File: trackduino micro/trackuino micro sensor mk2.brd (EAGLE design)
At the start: 43.3 x 19 mm, 44 parts, among them IC2 74AHC1G125DBV, SW1 SPST_TACT-KMR2, U1 ATMEGA168MLF, Y1 16MHZ

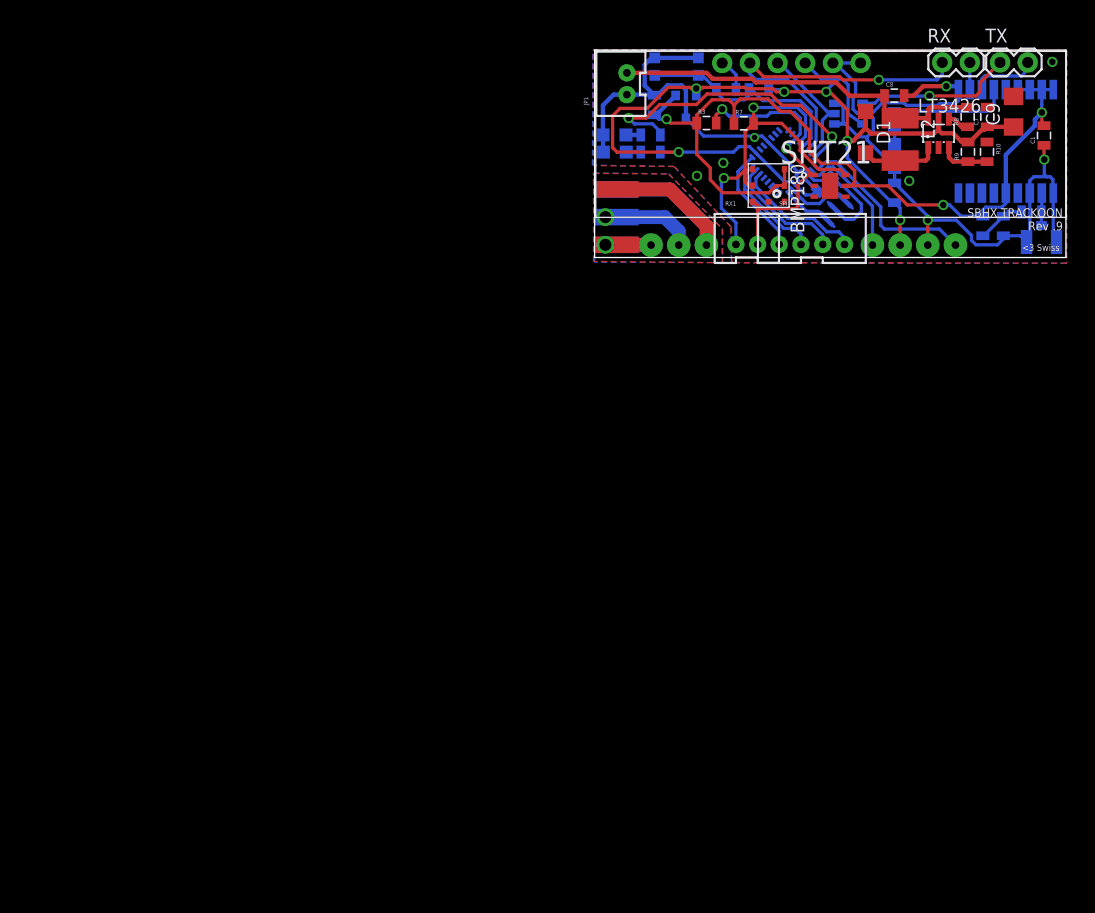
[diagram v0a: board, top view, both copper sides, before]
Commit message: Moved all boards to origin
Moved all the boards such that the lower left most corner is at the
origin.
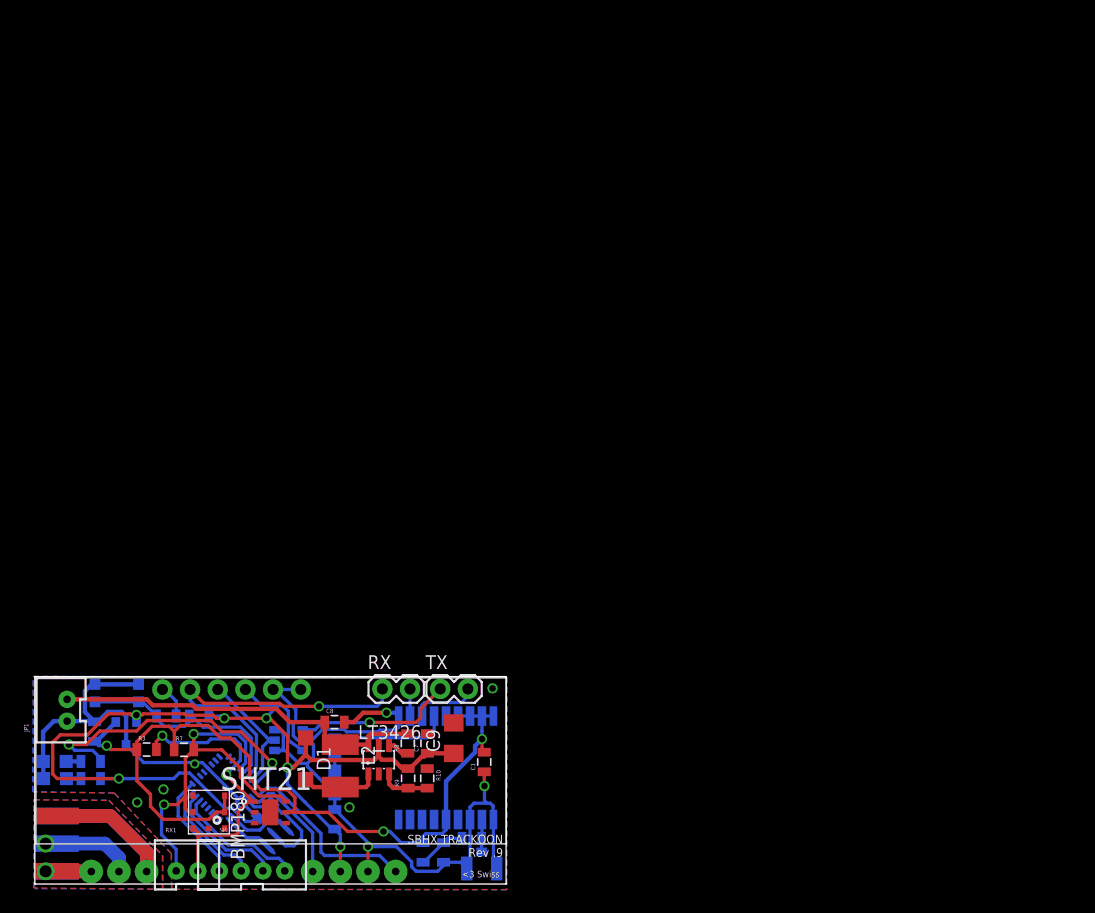
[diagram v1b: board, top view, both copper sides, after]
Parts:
- moved C5 77.1 mm to (12.1, 15.4)
- moved R4 77.1 mm to (5.13, 9.68)
- moved R5 77.1 mm to (15.1, 15.4)
- moved VCC 77.1 mm to (1.85, 9.68)
- moved BMP180 77.1 mm to (16.0, 6.60)
- moved C1 77.1 mm to (41.2, 11.2)
- moved C2 77.1 mm to (5.49, 14.0)
- moved C3 77.1 mm to (21.2, 6.76)
- moved C4 77.1 mm to (27.5, 5.94)
- moved C6 77.1 mm to (37.5, 2.90)
- moved C7 77.1 mm to (36.0, 12.9)
- moved C8 77.1 mm to (27.5, 14.9)
- moved C9 77.1 mm to (38.5, 13.4)
- moved D1 77.1 mm to (24.9, 11.5)
- moved FRAME1 77.1 mm to (14.4, -8.15)
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
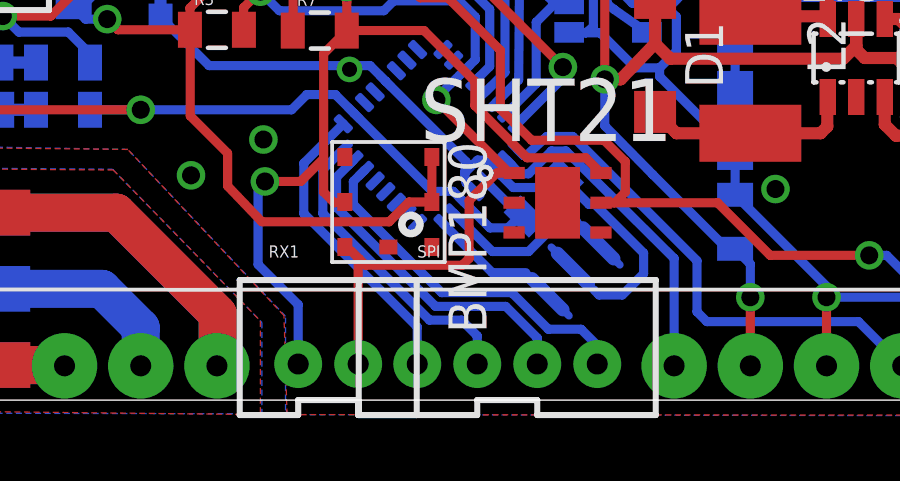
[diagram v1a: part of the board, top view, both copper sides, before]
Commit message: lined up 12c / spi headers
lined up api and i2c headers between the chip, u.fl, and solar versions
of the board.
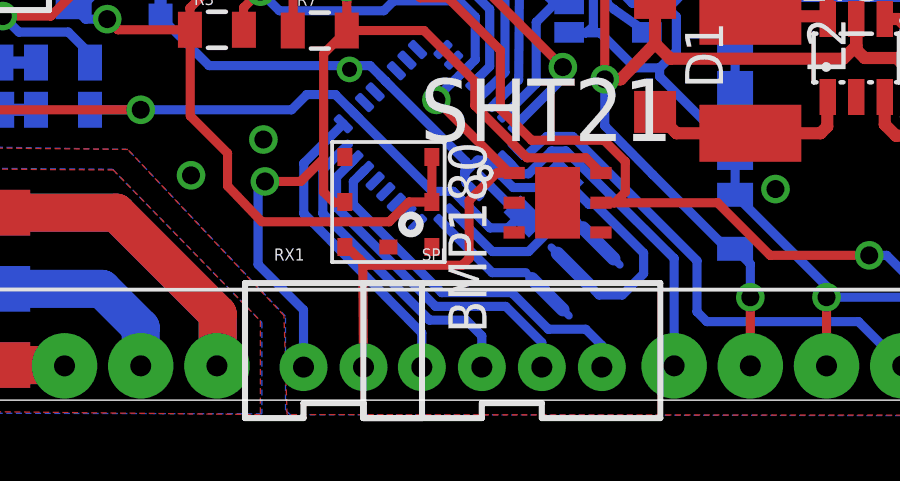
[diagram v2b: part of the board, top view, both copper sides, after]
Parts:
- moved RX1 0.20 mm to (14.1, 1.65)
- moved SPI 0.18 mm to (20.1, 1.65)
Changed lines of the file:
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@@
 <element name="C5" library="SparkFun-Capacitors" package="0805" value=".1uf" x="12.071159375" y="15.427575" rot="MR0"/>
 <element name="TX" library="SparkFun-Connectors" package="1X02" value="TX" x="37.211" y="17.907"/>
-<element name="SPI" library="SparkFun-Connectors" package="JST-4-PTH-VERT" value="" x="19.939" y="1.7526"/>
+<element name="SPI" library="SparkFun-Connectors" package="JST-4-PTH-VERT" value="" x="20.0914" y="1.651"/>
 <element name="FRAME1" library="SparkFun-Aesthetics" package="CREATIVE_COMMONS" value="FRAME-LETTER" x="14.3764" y="-8.1534"/>
 <element name="PTT" library="adafruit" package="CHIP-LED0805" value="" x="1.8288" y="11.2522" rot="MR270"/>
@@
 <attribute name="OC_FARNELL" value="1855468" x="21.6154" y="6.5786" size="1.778" layer="27" display="off"/>
 </element>
-<element name="RX1" library="SparkFun-Connectors" package="JST-2-PTH-VERT" value="RX" x="13.97" y="1.7526"/>
+<element name="RX1" library="SparkFun-Connectors" package="JST-2-PTH-VERT" value="RX" x="14.1478" y="1.651"/>
 </elements>
 <signals>
@@
 <contactref element="U1" pad="16"/>
 <contactref element="SPI" pad="2"/>
-<wire x1="18.939" y1="1.2026" x2="18.939" y2="2.143" width="0.3048" layer="16"/>
-<wire x1="18.939" y1="2.143" x2="18.415" y2="2.667" width="0.3048" layer="16"/>
-<wire x1="18.415" y1="2.667" x2="17.3482" y2="2.667" width="0.3048" layer="16"/>
+<wire x1="19.0914" y1="1.101" x2="19.0914" y2="2.143" width="0.3048" layer="16"/>
+<wire x1="19.0914" y1="2.143" x2="18.5674" y2="2.667" width="0.3048" layer="16"/>
+<wire x1="18.5674" y1="2.667" x2="17.3482" y2="2.667" width="0.3048" layer="16"/>
 <wire x1="17.3482" y1="2.667" x2="13.7922" y2="6.223" width="0.3048" layer="16"/>
 <wire x1="13.7922" y1="6.223" x2="13.7922" y2="7.681871875" width="0.3048" layer="16"/>
@@
 <contactref element="U1" pad="15"/>
 <contactref element="SPI" pad="3"/>
-<wire x1="20.939" y1="1.2026" x2="20.939" y2="2.0734" width="0.3048" layer="16"/>
-<wire x1="20.939" y1="2.0734" x2="19.8882" y2="3.1242" width="0.3048" layer="16"/>
+<wire x1="21.0914" y1="1.101" x2="21.0914" y2="1.921" width="0.3048" layer="16"/>
+<wire x1="21.0914" y1="1.921" x2="19.8882" y2="3.1242" width="0.3048" layer="16"/>
 <wire x1="19.8882" y1="3.1242" x2="17.5514" y2="3.1242" width="0.3048" layer="16"/>
 <wire x1="17.5514" y1="3.1242" x2="14.2494" y2="6.4262" width="0.3048" layer="16"/>
@@
 <contactref element="U1" pad="17"/>
 <contactref element="SPI" pad="1"/>
-<wire x1="16.939" y1="1.2026" x2="16.939" y2="2.4412" width="0.3048" layer="16"/>
-<wire x1="16.939" y1="2.4412" x2="13.1572" y2="6.223" width="0.3048" layer="16"/>
+<wire x1="17.0914" y1="1.101" x2="17.0914" y2="2.238" width="0.3048" layer="16"/>
+<wire x1="17.0914" y1="2.238" x2="13.1572" y2="6.223" width="0.3048" layer="16"/>
 <wire x1="13.1572" y1="6.223" x2="13.1572" y2="7.8954" width="0.3048" layer="16"/>
 <wire x1="13.1572" y1="7.8954" x2="14.4744625" y2="9.2126625" width="0.3048" layer="16"/>
@@
 <contactref element="U1" pad="14"/>
 <contactref element="SPI" pad="4"/>
-<wire x1="22.939" y1="1.2026" x2="22.939" y2="1.826" width="0.3048" layer="16"/>
-<wire x1="22.939" y1="1.826" x2="22.4028" y2="2.3622" width="0.3048" layer="16"/>
-<wire x1="22.4028" y1="2.3622" x2="21.3106" y2="2.3622" width="0.3048" layer="16"/>
+<wire x1="23.0914" y1="1.101" x2="23.0914" y2="1.826" width="0.3048" layer="16"/>
+<wire x1="23.0914" y1="1.826" x2="22.5552" y2="2.3622" width="0.3048" layer="16"/>
+<wire x1="22.5552" y1="2.3622" x2="21.3106" y2="2.3622" width="0.3048" layer="16"/>
 <wire x1="21.3106" y1="2.3622" x2="20.0914" y2="3.5814" width="0.3048" layer="16"/>
 <wire x1="20.0914" y1="3.5814" x2="17.7546" y2="3.5814" width="0.3048" layer="16"/>
@@
 <wire x1="17.5768" y1="10.07765625" x2="18.504971875" y2="10.980428125" width="0.3048" layer="16"/>
 <contactref element="RX1" pad="2"/>
-<wire x1="14.97" y1="1.2026" x2="14.97" y2="4.683" width="0.3048" layer="1"/>
-<wire x1="14.97" y1="4.683" x2="14.9987" y2="4.7117" width="0.3048" layer="1"/>
+<wire x1="15.1478" y1="1.101" x2="15.1224" y2="4.5814" width="0.3048" layer="1"/>
+<wire x1="15.1224" y1="4.5814" x2="14.9987" y2="4.7117" width="0.3048" layer="1"/>
 </signal>
 <signal name="SCL">
@@
 <wire x1="17.1664" y1="12.319" x2="14.5906" y2="12.319" width="0.3048" layer="1"/>
 <contactref element="RX1" pad="1"/>
-<wire x1="12.97" y1="1.2026" x2="12.97" y2="3.1844" width="0.3048" layer="16"/>
-<wire x1="12.97" y1="3.1844" x2="11.6332" y2="4.5212" width="0.3048" layer="16"/>
+<wire x1="13.1478" y1="1.101" x2="13.1478" y2="3.0066" width="0.3048" layer="16"/>
+<wire x1="13.1478" y1="3.0066" x2="11.6332" y2="4.5212" width="0.3048" layer="16"/>
 <wire x1="11.6332" y1="4.5212" x2="11.6332" y2="7.0612" width="0.3048" layer="16"/>
 <wire x1="11.6332" y1="7.0612" x2="11.8618" y2="7.2898" width="0.3048" layer="16"/>

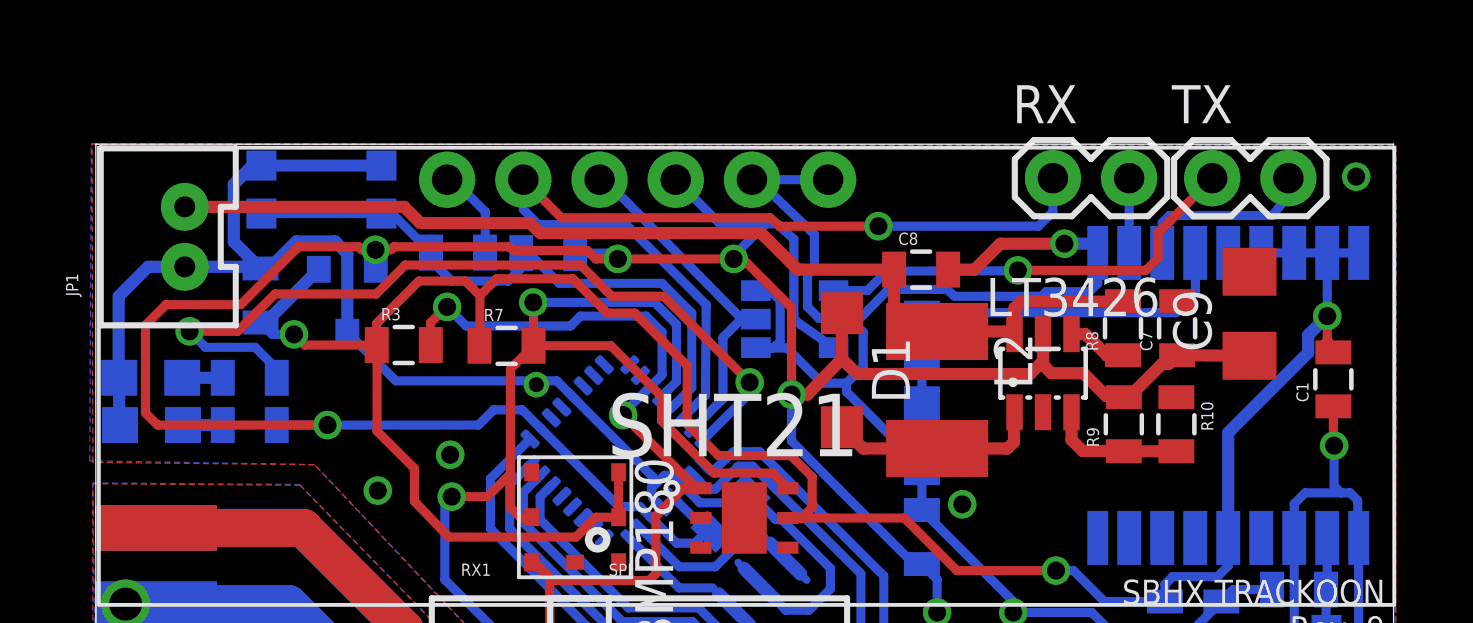
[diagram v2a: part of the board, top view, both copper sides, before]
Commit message: tx rx 2mm headers
replaced .1” serial headers on chip and non chip version with 2mm
headers
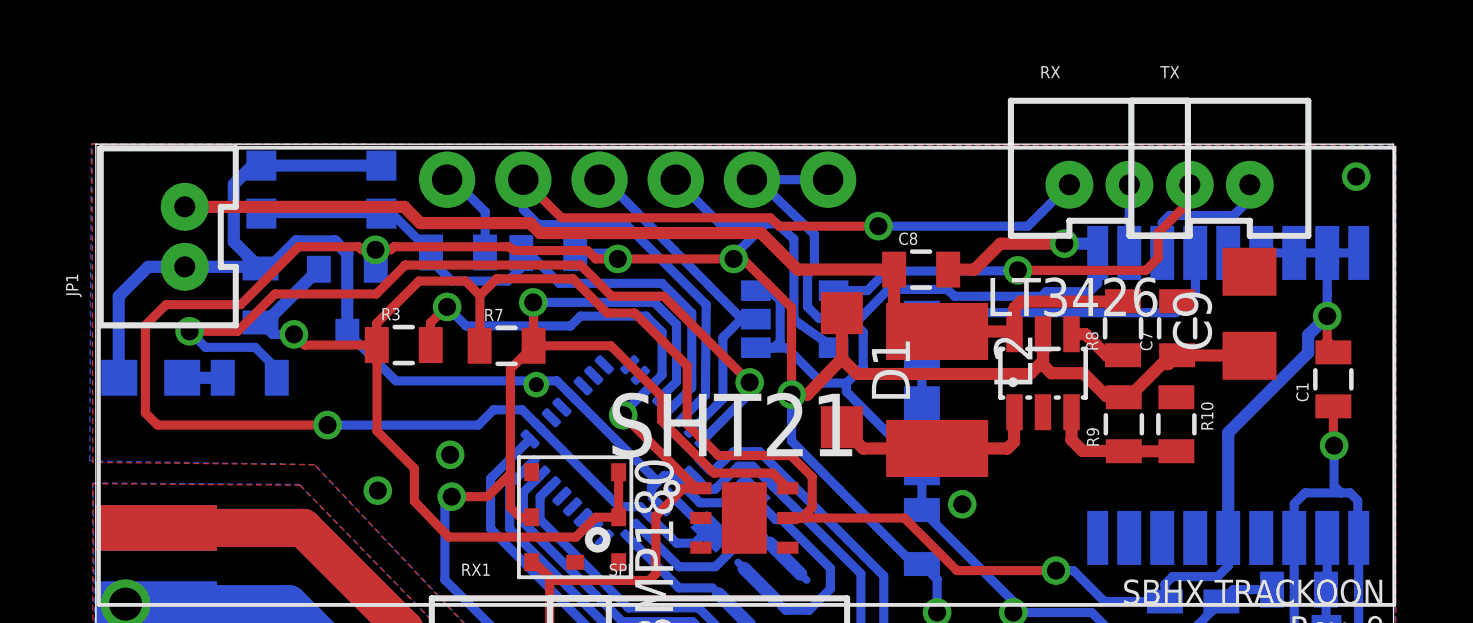
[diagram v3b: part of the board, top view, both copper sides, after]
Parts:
- removed R4: 330ohm, SparkFun-Resistors:0805
- removed VCC: (no value), adafruit:CHIP-LED0805
- RX, TX: device SparkFun-Connectors:1X02 -> SparkFun-Connectors:JST-2-PTH-VERT
- moved RX 1.58 mm to (33.5, 18.2)
- moved TX 0.42 mm to (37.5, 18.2)
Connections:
- removed net N$8: R4.1, VCC.A
- net GND: no longer VCC.C
- net VCC: no longer R4.2
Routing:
- net VCC: track 99.2 -> 97.5 mm
- net GND: track 150.5 -> 148.9 mm
- net RX: track 6.21 -> 4.73 mm
- net N$8: track 1.33 -> 0.00 mm
- net TX1: track 14.7 -> 14.1 mm
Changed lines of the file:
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@@
 <element name="C3" library="SparkFun-Capacitors" package="0805" value=".1uf" x="21.1582" y="6.7564" rot="MR315"/>
 <element name="C4" library="SparkFun-Capacitors" package="0805" value=".1uf" x="27.5336" y="5.9436" rot="MR270"/>
-<element name="VCC" library="adafruit" package="CHIP-LED0805" value="" x="1.8542" y="9.6774" rot="MR270"/>
-<element name="R4" library="SparkFun-Resistors" package="0805" value="330ohm" x="5.1308" y="9.6774" rot="MR180"/>
 <element name="FTDI" library="SparkFun-Connectors" package="1X06_NO_SILK" value="" x="11.7094" y="17.8562" rot="MR180">
 <attribute name="PROD_ID" value="CONN-08437" x="11.7094" y="17.8562" size="1.778" layer="28" rot="MR180" display="off"/>
@@
 <element name="R5" library="SparkFun-Resistors" package="0805" value="10k" x="15.077075" y="15.407278125" rot="MR180"/>
 <element name="C5" library="SparkFun-Capacitors" package="0805" value=".1uf" x="12.071159375" y="15.427575" rot="MR0"/>
-<element name="TX" library="SparkFun-Connectors" package="1X02" value="TX" x="37.211" y="17.907"/>
+<element name="TX" library="SparkFun-Connectors" package="JST-2-PTH-VERT" value="TX" x="37.465" y="18.2372"/>
 <element name="SPI" library="SparkFun-Connectors" package="JST-4-PTH-VERT" value="" x="20.0914" y="1.651"/>
 <element name="FRAME1" library="SparkFun-Aesthetics" package="CREATIVE_COMMONS" value="FRAME-LETTER" x="14.3764" y="-8.1534"/>
@@
 <element name="R2" library="SparkFun-Resistors" package="0805" value="10ohm" x="35.6362" y="2.8956" rot="MR90"/>
 <element name="C6" library="SparkFun-Capacitors" package="0805" value="47pf" x="37.5158" y="2.8956" rot="MR270"/>
-<element name="RX" library="SparkFun-Connectors" package="1X02" value="RX" x="31.9024" y="17.907"/>
+<element name="RX" library="SparkFun-Connectors" package="JST-2-PTH-VERT" value="RX" x="33.4518" y="18.2372"/>
 <element name="BMP180" library="SparkFun-Sensors" package="BMP180" value="BMP180" x="15.9766" y="6.604" rot="R270"/>
 <element name="R3" library="SparkFun-Resistors" package="0805" value="4.7k" x="10.2616" y="12.3444"/>
@@
 <contactref element="C3" pad="1"/>
 <contactref element="C4" pad="1"/>
-<contactref element="VCC" pad="C"/>
 <contactref element="U1" pad="3"/>
 <contactref element="U1" pad="5"/>
@@
 <wire x1="0.762" y1="13.97" x2="0.762" y2="11.269" width="0.4064" layer="16"/>
 <wire x1="0.762" y1="11.269" x2="0.7788" y2="11.2522" width="0.4064" layer="16"/>
-<wire x1="0.7788" y1="11.2522" x2="0.7788" y2="9.7028" width="0.4064" layer="16"/>
-<wire x1="0.7788" y1="9.7028" x2="0.8042" y2="9.6774" width="0.4064" layer="16"/>
 <wire x1="2.963" y1="14.9512" x2="5.4306" y2="14.9512" width="0.4064" layer="16"/>
 <wire x1="5.4306" y1="14.9512" x2="5.4864" y2="14.8954" width="0.4064" layer="16"/>
@@
 <contactref element="C3" pad="2"/>
 <contactref element="C4" pad="2"/>
-<contactref element="R4" pad="2"/>
 <contactref element="U1" pad="4"/>
 <contactref element="U1" pad="6"/>
@@
 <wire x1="13.2588" y1="10.1854" x2="12.7508" y2="9.6774" width="0.3048" layer="16"/>
 <wire x1="12.7508" y1="9.6774" x2="7.7216" y2="9.6774" width="0.3048" layer="16"/>
-<wire x1="7.7216" y1="9.6774" x2="6.0308" y2="9.6774" width="0.3048" layer="16"/>
 <wire x1="14.828015625" y1="9.566215625" x2="17.43463125" y2="6.9596" width="0.3048" layer="16"/>
 <wire x1="17.43463125" y1="6.9596" x2="18.1356" y2="6.9596" width="0.3048" layer="16"/>
@@
 <contactref element="U$1" pad="2_TXD1"/>
 <contactref element="RX" pad="2"/>
-<wire x1="34.4424" y1="17.907" x2="34.4424" y2="15.5192" width="0.3048" layer="16"/>
+<wire x1="34.4518" y1="17.6872" x2="34.4424" y2="15.5192" width="0.3048" layer="16"/>
 <wire x1="34.4424" y1="15.5192" x2="34.4452" y2="15.4148" width="0.3048" layer="16"/>
 </signal>
@@
 <wire x1="35.5452" y1="15.4148" x2="35.5452" y2="16.419" width="0.3048" layer="16"/>
 <wire x1="35.5452" y1="16.419" x2="35.7886" y2="16.6624" width="0.3048" layer="16"/>
-<wire x1="35.7886" y1="16.6624" x2="39.2176" y2="16.6624" width="0.3048" layer="16"/>
-<wire x1="39.2176" y1="16.6624" x2="39.751" y2="17.3228" width="0.3048" layer="16"/>
-<wire x1="39.751" y1="17.3228" x2="39.751" y2="17.907" width="0.3048" layer="16"/>
-</signal>
-<signal name="N$8">
-<contactref element="VCC" pad="A"/>
-<contactref element="R4" pad="1"/>
-<wire x1="2.9042" y1="9.6774" x2="4.2308" y2="9.6774" width="0.4064" layer="16"/>
+<wire x1="35.7886" y1="16.6624" x2="37.9222" y2="16.6624" width="0.3048" layer="16"/>
+<wire x1="37.9222" y1="16.6624" x2="38.4556" y2="17.1958" width="0.3048" layer="16"/>
+<wire x1="38.4556" y1="17.1958" x2="38.465" y2="17.6872" width="0.3048" layer="16"/>
 </signal>
 <signal name="DTR">
@@
 <wire x1="14.7574" y1="16.3576" x2="14.2494" y2="16.8656" width="0.3048" layer="16"/>
 <wire x1="14.2494" y1="16.8656" x2="14.2494" y2="17.8562" width="0.3048" layer="16"/>
-<wire x1="31.9024" y1="17.907" x2="31.9024" y2="16.7894" width="0.3048" layer="16"/>
-<wire x1="31.9024" y1="16.7894" x2="31.4198" y2="16.3068" width="0.3048" layer="16"/>
-<wire x1="31.4198" y1="16.3068" x2="26.0858" y2="16.3068" width="0.3048" layer="16"/>
+<wire x1="32.4518" y1="17.6872" x2="31.5468" y2="16.7894" width="0.3048" layer="16"/>
+<wire x1="31.5468" y1="16.7894" x2="31.0642" y2="16.3068" width="0.3048" layer="16"/>
+<wire x1="31.0642" y1="16.3068" x2="26.0858" y2="16.3068" width="0.3048" layer="16"/>
 <via x="26.0858" y="16.3068" extent="1-16" drill="0.6" shape="square"/>
 <wire x1="26.0858" y1="16.3068" x2="22.7838" y2="16.3068" width="0.3048" layer="1"/>
@@
 <wire x1="35.0012" y1="14.8336" x2="35.4076" y2="15.24" width="0.3048" layer="1"/>
 <wire x1="35.4076" y1="15.24" x2="35.4076" y2="16.0782" width="0.3048" layer="1"/>
-<wire x1="35.4076" y1="16.0782" x2="35.7886" y2="16.4592" width="0.3048" layer="1"/>
-<wire x1="35.7886" y1="16.4592" x2="37.211" y2="17.907" width="0.3048" layer="1"/>
+<wire x1="35.4076" y1="16.0782" x2="36.4744" y2="17.145" width="0.3048" layer="1"/>
+<wire x1="36.4744" y1="17.145" x2="36.465" y2="17.6872" width="0.3048" layer="1"/>
 </signal>
 <signal name="VDDD">
